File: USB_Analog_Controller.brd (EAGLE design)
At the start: 50 x 36 mm, 20 parts, among them J1 POWER, Q1 AO3400, Q2 AO3400, U1 PICO-MINI-02, U2 AP2112K, X1 PROG, X2 LED1, X3 LED2, X5 BOOT, X6 RESET

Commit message: Revision 2023-07-17
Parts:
- added R5, R6: 10K, M2M-Passives:R0603
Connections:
- net EN: now also R6.1
- net IO0: now also R5.1
- net L1: now also U1.12; no longer U1.9
- net L2: now also U1.13; no longer U1.10
- net VCC: now also R5.2, R6.2
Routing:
- net VCC: track 22.5 -> 33.6 mm
- net L1: track 10.8 -> 15.8 mm
- net EN: track 25.2 -> 26.8 mm
- net IO0: track 30.8 -> 32.2 mm
- net L2: track 13.6 -> 14.2 mm
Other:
- board text added: "2023-07-17"
- board text removed: "2023-06-03"
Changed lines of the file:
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@@
 <wire x1="23.5" y1="36" x2="2" y2="36" width="0" layer="20"/>
 <wire x1="2" y1="36" x2="0" y2="34" width="0" layer="20" curve="90"/>
-<text x="48.5" y="7" size="1.27" layer="21" rot="R90">USB Analog Controller</text>
-<text x="15.5" y="33.5" size="1.27" layer="21">2023-06-03</text>
+<text x="48.5" y="6" size="1.27" layer="21" rot="R90">USB Analog
+Controller</text>
+<text x="48.5" y="20" size="1.016" layer="21" rot="R90">2023-07-17</text>
 </plain>
 <attributes>
@@
 <attribute name="NAME" x="29.9275" y="2.23" size="1.016" layer="26" rot="R90"/>
 <attribute name="NAME" x="38.5" y="4.135" size="1.27" layer="51" rot="R180" align="bottom-center"/>
-<attribute name="VALUE" x="30.73" y="0.975" size="1.016" layer="27"/>
+<attribute name="VALUE" x="30.73" y="0.975" size="1.016" layer="21"/>
 </element>
 <element name="X2" library="M2M-Connectors" package="USB-A-SS-52100-001" value="LED1" x="10" y="27" smashed="yes" rot="R90">
@@
 </element>
 <element name="X5" library="M2M-Connectors" package="1X02-2.54" value="BOOT" x="25.5" y="3.5" smashed="yes">
-<attribute name="NAME" x="24.611" y="2.865" size="1.27" layer="48"/>
 <attribute name="NAME" x="24.865" y="2.865" size="0.8128" layer="51"/>
 <attribute name="NAME" x="24.23" y="5.0875" size="1.016" layer="25"/>
-<attribute name="VALUE" x="24.23" y="0.96" size="1.016" layer="27"/>
+<attribute name="NAME" x="24.611" y="2.865" size="1.27" layer="48"/>
+<attribute name="VALUE" x="24.23" y="0.96" size="1.016" layer="21"/>
 </element>
 <element name="X6" library="M2M-Connectors" package="1X02-2.54" value="RESET" x="19" y="3.5" smashed="yes">
-<attribute name="NAME" x="18.111" y="2.865" size="1.27" layer="48"/>
 <attribute name="NAME" x="18.865" y="2.365" size="0.8128" layer="51"/>
 <attribute name="NAME" x="17.73" y="5.0875" size="1.016" layer="25"/>
-<attribute name="VALUE" x="17.73" y="0.96" size="1.016" layer="27"/>
+<attribute name="NAME" x="18.111" y="2.865" size="1.27" layer="48"/>
+<attribute name="VALUE" x="17.73" y="0.96" size="1.016" layer="21"/>
 </element>
 <element name="J1" library="M2M-Connectors" package="TERMINAL-5.08-2P" value="POWER" x="36" y="11.5" smashed="yes"/>
@@
 <element name="U$1" library="M2M-Frames" package="BERGDAHL-20MM-BPLACE" value="" x="21" y="25.5" smashed="yes" rot="R270"/>
 <element name="U$2" library="M2M-Frames" package="OSHW-8MM-BPLACE" value="" x="35.5" y="17.5" smashed="yes" rot="R270"/>
+<element name="R5" library="M2M-Passives" package="R0603" value="10K" x="28.5" y="6.5" smashed="yes" rot="R180">
+<attribute name="NAME" x="28.5" y="5.5475" size="1.016" layer="25" rot="R180" align="bottom-center"/>
+<attribute name="NAME" x="28.5" y="6.5" size="0.6096" layer="51" rot="R180" align="center"/>
+<attribute name="VALUE" x="28.5" y="8.405" size="1.016" layer="27" rot="R180" align="bottom-center"/>
+</element>
+<element name="R6" library="M2M-Passives" package="R0603" value="10K" x="25.5" y="6.5" smashed="yes">
+<attribute name="NAME" x="25.5" y="7.4525" size="1.016" layer="25" align="bottom-center"/>
+<attribute name="NAME" x="25.5" y="6.5" size="0.6096" layer="51" align="center"/>
+<attribute name="VALUE" x="25.5" y="4.595" size="1.016" layer="27" align="bottom-center"/>
+</element>
 </elements>
 <signals>
@@
 <wire x1="29" y1="22.5" x2="24" y2="27.5" width="0.4064" layer="16"/>
 <wire x1="24" y1="27.5" x2="23.5" y2="27.5" width="0.4064" layer="16"/>
+<contactref element="R5" pad="2"/>
+<contactref element="R6" pad="2"/>
+<wire x1="26.35" y1="6.5" x2="26.5" y2="6.5" width="0.254" layer="1"/>
+<wire x1="26.5" y1="6.5" x2="27.65" y2="6.5" width="0.254" layer="1"/>
+<wire x1="26.55" y1="14.2" x2="24" y2="11.65" width="0.254" layer="1"/>
+<wire x1="24" y1="9" x2="26.5" y2="6.5" width="0.254" layer="1"/>
+<wire x1="24" y1="11.65" x2="24" y2="9" width="0.254" layer="1"/>
 </signal>
 <signal name="GND">
@@
 <via x="40" y="18.5" extent="1-16" drill="0.35"/>
 <via x="31" y="18.5" extent="1-16" drill="0.35"/>
-<via x="27" y="18.5" extent="1-16" drill="0.35"/>
+<via x="27.119" y="19.643" extent="1-16" drill="0.35"/>
 <via x="47.5" y="2.5" extent="1-16" drill="0.35"/>
 <via x="43.5" y="10.5" extent="1-16" drill="0.35"/>
@@
 <via x="9.5" y="8" extent="1-16" drill="0.35"/>
 <via x="29.5" y="16" extent="1-16" drill="0.35"/>
-<via x="29.5" y="7.5" extent="1-16" drill="0.35"/>
+<via x="31" y="8.5" extent="1-16" drill="0.35"/>
 <via x="25" y="10" extent="1-16" drill="0.35"/>
 <via x="21.5" y="8.5" extent="1-16" drill="0.35"/>
@@
 <wire x1="41" y1="7" x2="41" y2="16" width="0.254" layer="1"/>
 <wire x1="41" y1="16" x2="38" y2="19" width="0.254" layer="1"/>
-<wire x1="27.5" y1="5.5" x2="39.5" y2="5.5" width="0.254" layer="1"/>
+<wire x1="27.5" y1="5.5" x2="30.35" y2="5.5" width="0.254" layer="1"/>
+<contactref element="R5" pad="1"/>
+<wire x1="30.5" y1="5.5" x2="39.5" y2="5.5" width="0.254" layer="1"/>
+<wire x1="29.35" y1="6.5" x2="30.35" y2="5.5" width="0.254" layer="1"/>
+<wire x1="30.35" y1="5.5" x2="30.5" y2="5.5" width="0.254" layer="1"/>
 </signal>
 <signal name="EN">
 <contactref element="U1" pad="8"/>
 <contactref element="X6" pad="1"/>
-<wire x1="28.1" y1="22.9" x2="27.1" y2="22.9" width="0.254" layer="1"/>
-<wire x1="27.1" y1="22.9" x2="26.5" y2="23.5" width="0.254" layer="1"/>
-<via x="26.5" y="23.5" extent="1-16" drill="0.35"/>
-<wire x1="26.5" y1="23.5" x2="26.5" y2="20.5" width="0.254" layer="16"/>
-<via x="26.5" y="20.5" extent="1-16" drill="0.35"/>
+<wire x1="28.1" y1="22.9" x2="27.4" y2="22.9" width="0.254" layer="1"/>
+<wire x1="27.4" y1="22.9" x2="26.5" y2="22" width="0.254" layer="1"/>
+<via x="26.5" y="22" extent="1-16" drill="0.35"/>
+<wire x1="26.5" y1="22" x2="26.5" y2="17.5" width="0.254" layer="16"/>
+<via x="26.5" y="17.5" extent="1-16" drill="0.35"/>
 <wire x1="23" y1="7.5" x2="19" y2="3.5" width="0.254" layer="1"/>
-<wire x1="26.5" y1="20.5" x2="26" y2="20.5" width="0.254" layer="1"/>
-<wire x1="26" y1="20.5" x2="23" y2="17.5" width="0.254" layer="1"/>
-<wire x1="23" y1="17.5" x2="23" y2="7.5" width="0.254" layer="1"/>
+<wire x1="26.5" y1="17.5" x2="24.5" y2="17.5" width="0.254" layer="1"/>
+<wire x1="24.5" y1="17.5" x2="23" y2="16" width="0.254" layer="1"/>
+<wire x1="23" y1="16" x2="23" y2="7.5" width="0.254" layer="1"/>
+<contactref element="R6" pad="1"/>
+<wire x1="24.65" y1="6.5" x2="24" y2="6.5" width="0.254" layer="1"/>
+<wire x1="24" y1="6.5" x2="23" y2="7.5" width="0.254" layer="1"/>
 </signal>
 <signal name="TXD0">
@@
 </signal>
 <signal name="L1">
-<contactref element="U1" pad="9"/>
 <contactref element="R1" pad="1"/>
-<wire x1="26.9" y1="22.1" x2="28.1" y2="22.1" width="0.254" layer="1"/>
-<wire x1="19.35" y1="27" x2="22" y2="27" width="0.254" layer="1"/>
-<wire x1="22" y1="27" x2="26.9" y2="22.1" width="0.254" layer="1"/>
+<wire x1="21.5" y1="27" x2="19.35" y2="27" width="0.254" layer="1"/>
+<contactref element="U1" pad="12"/>
+<wire x1="29.2" y1="19.6" x2="29.2" y2="19.2132" width="0.254" layer="1"/>
+<wire x1="29.2" y1="19.2132" x2="28.5" y2="18.5132" width="0.254" layer="1"/>
+<wire x1="28.5" y1="18.5132" x2="26.9868" y2="18.5132" width="0.254" layer="1"/>
+<wire x1="26.9868" y1="18.5132" x2="25" y2="20.5" width="0.254" layer="1"/>
+<wire x1="25" y1="20.5" x2="25" y2="23.5" width="0.254" layer="1"/>
+<wire x1="25" y1="23.5" x2="21.5" y2="27" width="0.254" layer="1"/>
 </signal>
 <signal name="L2">
-<contactref element="U1" pad="10"/>
 <contactref element="R2" pad="1"/>
-<wire x1="28.1" y1="21.3" x2="25.3" y2="21.3" width="0.254" layer="1"/>
-<wire x1="19.35" y1="15.35" x2="19.35" y2="13" width="0.254" layer="1"/>
-<wire x1="25.3" y1="21.3" x2="19.35" y2="15.35" width="0.254" layer="1"/>
+<wire x1="19.35" y1="13" x2="19.35" y2="13.85" width="0.254" layer="1"/>
+<contactref element="U1" pad="13"/>
+<wire x1="30" y1="19" x2="30" y2="19.6" width="0.254" layer="1"/>
+<wire x1="19.35" y1="13.85" x2="23.6068" y2="18.1068" width="0.254" layer="1"/>
+<wire x1="23.6068" y1="18.1068" x2="29.1068" y2="18.1068" width="0.254" layer="1"/>
+<wire x1="29.1068" y1="18.1068" x2="30" y2="19" width="0.254" layer="1"/>
 </signal>
 <signal name="NC">

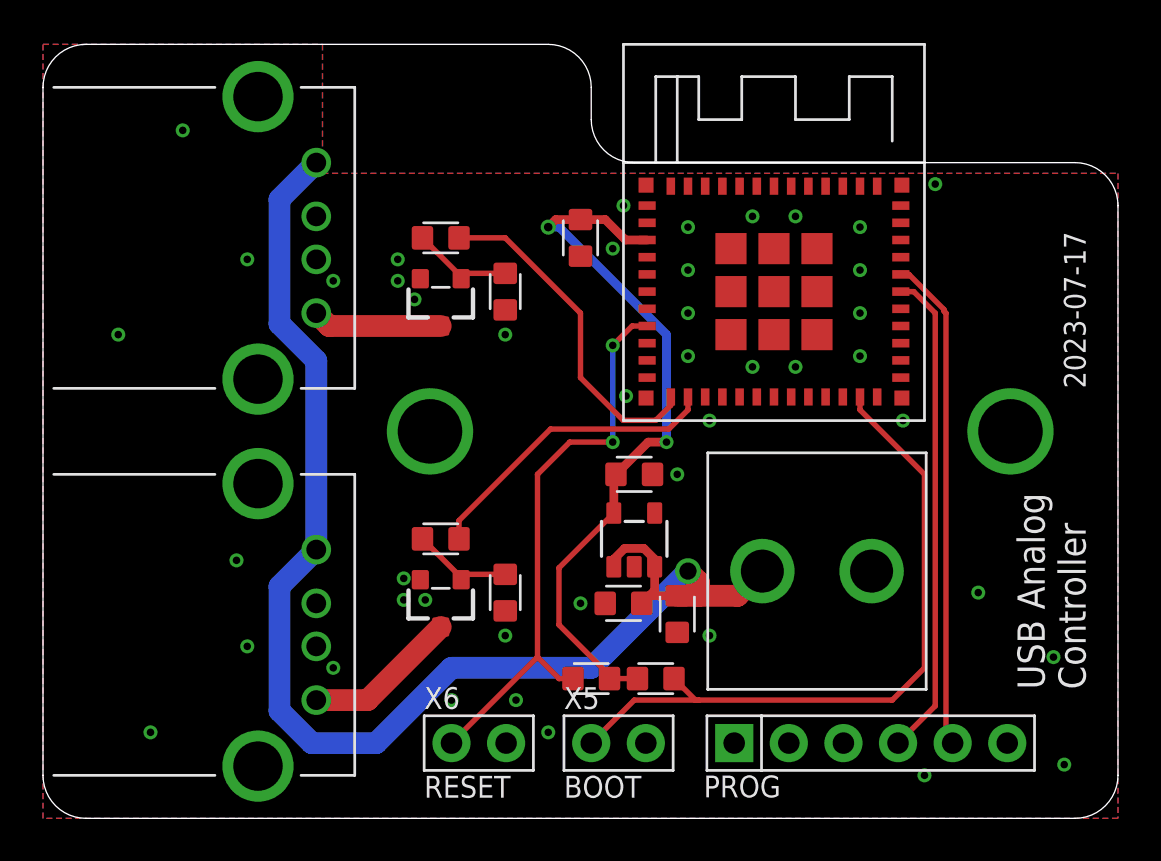
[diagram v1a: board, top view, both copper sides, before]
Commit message: Added PTC fuse
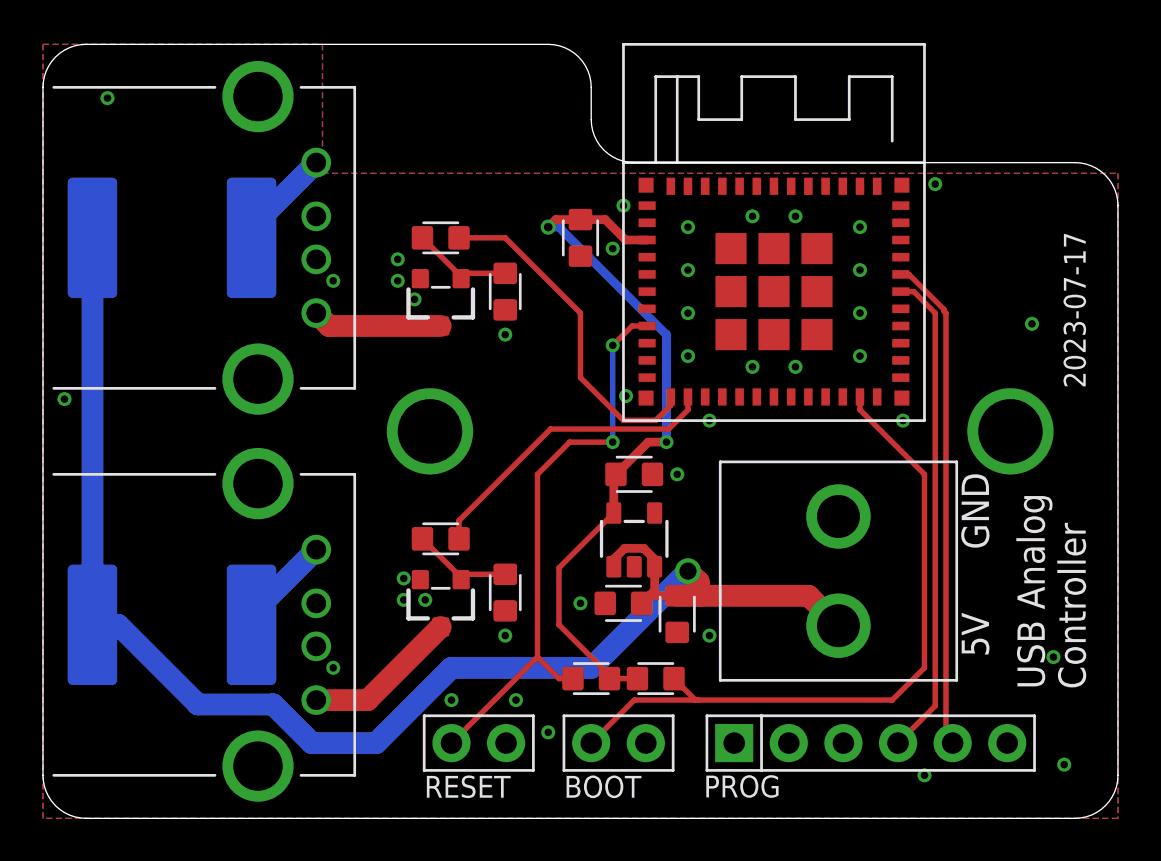
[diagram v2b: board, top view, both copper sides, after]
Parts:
- added F1, F2: 3A, M2M-Fuse:JK-SMD300
- moved J1 1.00 mm to (37.0, 11.5), turned to 90 degrees
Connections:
- new net N$5: F1.B, X2.1
- new net N$6: F2.B, X3.1
- net VIN: now also F1.A, F2.A; no longer X2.1, X3.1
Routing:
- net N$6: track 0.00 -> 4.75 mm
- net N$5: track 0.00 -> 4.75 mm
- net VIN: track 63.1 -> 67.5 mm
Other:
- board text added: "5V"
- board text added: "GND"
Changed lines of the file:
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@@
 Controller</text>
 <text x="48.5" y="20" size="1.016" layer="21" rot="R90">2023-07-17</text>
+<text x="44" y="12.5" size="1.27" layer="21" rot="R90">GND</text>
+<text x="44" y="7.5" size="1.27" layer="21" rot="R90">5V</text>
 </plain>
 <attributes>
@@
 </element>
 <element name="X5" library="M2M-Connectors" package="1X02-2.54" value="BOOT" x="25.5" y="3.5" smashed="yes">
-<attribute name="NAME" x="24.865" y="2.865" size="0.8128" layer="51"/>
 <attribute name="NAME" x="24.23" y="5.0875" size="1.016" layer="25"/>
 <attribute name="NAME" x="24.611" y="2.865" size="1.27" layer="48"/>
+<attribute name="NAME" x="24.865" y="2.865" size="0.8128" layer="51"/>
 <attribute name="VALUE" x="24.23" y="0.96" size="1.016" layer="21"/>
 </element>
 <element name="X6" library="M2M-Connectors" package="1X02-2.54" value="RESET" x="19" y="3.5" smashed="yes">
-<attribute name="NAME" x="18.865" y="2.365" size="0.8128" layer="51"/>
 <attribute name="NAME" x="17.73" y="5.0875" size="1.016" layer="25"/>
 <attribute name="NAME" x="18.111" y="2.865" size="1.27" layer="48"/>
+<attribute name="NAME" x="18.865" y="2.365" size="0.8128" layer="51"/>
 <attribute name="VALUE" x="17.73" y="0.96" size="1.016" layer="21"/>
 </element>
-<element name="J1" library="M2M-Connectors" package="TERMINAL-5.08-2P" value="POWER" x="36" y="11.5" smashed="yes"/>
+<element name="J1" library="M2M-Connectors" package="TERMINAL-5.08-2P" value="POWER" x="37" y="11.5" smashed="yes" rot="R90"/>
 <element name="U2" library="M2M-IC" package="SOT23-5" value="AP2112K" x="27.5" y="13" smashed="yes">
 <attribute name="NAME" x="27.495" y="14.805" size="1.016" layer="25" align="bottom-center"/>
@@
 <attribute name="NAME" x="25.5" y="6.5" size="0.6096" layer="51" align="center"/>
 <attribute name="VALUE" x="25.5" y="4.595" size="1.016" layer="27" align="bottom-center"/>
+</element>
+<element name="F1" library="M2M-Fuse" package="JK-SMD300" value="3A" x="6" y="27" smashed="yes" rot="MR180">
+<attribute name="NAME" x="1" y="23.5" size="1.016" layer="26" rot="MR180"/>
+<attribute name="NAME" x="6" y="27" size="1.016" layer="48" rot="MR180" align="center"/>
+<attribute name="VALUE" x="1" y="31.5" size="1.016" layer="28" rot="MR180"/>
+</element>
+<element name="F2" library="M2M-Fuse" package="JK-SMD300" value="3A" x="6" y="9" smashed="yes" rot="MR180">
+<attribute name="NAME" x="1" y="5.5" size="1.016" layer="26" rot="MR180"/>
+<attribute name="NAME" x="6" y="9" size="1.016" layer="48" rot="MR180" align="center"/>
+<attribute name="VALUE" x="1" y="13.5" size="1.016" layer="28" rot="MR180"/>
 </element>
 </elements>
@@
 <via x="27.119" y="19.643" extent="1-16" drill="0.35"/>
 <via x="47.5" y="2.5" extent="1-16" drill="0.35"/>
-<via x="43.5" y="10.5" extent="1-16" drill="0.35"/>
+<via x="46" y="23" extent="1-16" drill="0.35"/>
 <via x="47" y="7.5" extent="1-16" drill="0.35"/>
 <via x="41" y="2" extent="1-16" drill="0.35"/>
@@
 <via x="22" y="5.5" extent="1-16" drill="0.35"/>
 <via x="19" y="5.5" extent="1-16" drill="0.35"/>
-<via x="5" y="4" extent="1-16" drill="0.35"/>
-<via x="9" y="12" extent="1-16" drill="0.35"/>
-<via x="3.5" y="22.5" extent="1-16" drill="0.35"/>
-<via x="6.5" y="32" extent="1-16" drill="0.35"/>
+<via x="1" y="19.5" extent="1-16" drill="0.35"/>
+<via x="3" y="33.5" extent="1-16" drill="0.35"/>
 <via x="16.5" y="25" extent="1-16" drill="0.35"/>
 <via x="16.5" y="26" extent="1-16" drill="0.35"/>
@@
 <via x="13.5" y="7" extent="1-16" drill="0.35"/>
 <via x="13.5" y="25" extent="1-16" drill="0.35"/>
-<via x="9.5" y="26" extent="1-16" drill="0.35"/>
-<via x="9.5" y="8" extent="1-16" drill="0.35"/>
 <via x="29.5" y="16" extent="1-16" drill="0.35"/>
 <via x="31" y="8.5" extent="1-16" drill="0.35"/>
@@
 <contactref element="C3" pad="1"/>
 <contactref element="U2" pad="3"/>
-<contactref element="X2" pad="1"/>
-<contactref element="X3" pad="1"/>
 <contactref element="C2" pad="1"/>
-<wire x1="33.46" y1="11.5" x2="32.31" y2="10.35" width="1.016" layer="1"/>
-<wire x1="32.31" y1="10.35" x2="30.5" y2="10.35" width="1.016" layer="1"/>
 <wire x1="30.5" y1="10.35" x2="29.5" y2="10.35" width="1.016" layer="1"/>
 <via x="30" y="11.5" extent="1-16" drill="0.8"/>
@@
 <wire x1="27.85" y1="10" x2="28.2" y2="10.35" width="0.4064" layer="1"/>
 <wire x1="28.2" y1="10.35" x2="29.5" y2="10.35" width="0.4064" layer="1"/>
-<wire x1="12.71" y1="12.5" x2="12.71" y2="21.29" width="1.016" layer="16"/>
-<wire x1="11" y1="23" x2="11" y2="28.79" width="1.016" layer="16"/>
-<wire x1="11" y1="28.79" x2="12.71" y2="30.5" width="1.016" layer="16"/>
-<wire x1="12.71" y1="21.29" x2="11" y2="23" width="1.016" layer="16"/>
-<wire x1="12.71" y1="12.5" x2="11" y2="10.79" width="1.016" layer="16"/>
-<wire x1="11" y1="10.79" x2="11" y2="5" width="1.016" layer="16"/>
-<wire x1="11" y1="5" x2="12.5" y2="3.5" width="1.016" layer="16"/>
 <wire x1="12.5" y1="3.5" x2="15.5" y2="3.5" width="1.016" layer="16"/>
 <wire x1="25.5" y1="7" x2="30" y2="11.5" width="1.016" layer="16"/>
@@
 <wire x1="28.45" y1="12.0516375" x2="27.9460375" y2="12.5556" width="0.4064" layer="1"/>
 <wire x1="27.9460375" y1="12.5556" x2="27.0539625" y2="12.5556" width="0.4064" layer="1"/>
+<contactref element="F1" pad="A"/>
+<contactref element="F2" pad="A"/>
+<wire x1="10.7" y1="5.3" x2="12.5" y2="3.5" width="1.016" layer="16"/>
+<wire x1="2.3" y1="27" x2="2.3" y2="9" width="1.016" layer="16"/>
+<wire x1="2.3" y1="9" x2="3.5" y2="9" width="1.016" layer="16"/>
+<wire x1="7.2" y1="5.3" x2="10.7" y2="5.3" width="1.016" layer="16"/>
+<wire x1="3.5" y1="9" x2="7.2" y2="5.3" width="1.016" layer="16"/>
+<wire x1="35.61" y1="10.35" x2="37" y2="8.96" width="1.016" layer="1"/>
+<wire x1="30.5" y1="10.35" x2="35.61" y2="10.35" width="1.016" layer="1"/>
+</signal>
+<signal name="N$5">
+<contactref element="X2" pad="1"/>
+<contactref element="F1" pad="B"/>
+<wire x1="12.71" y1="30.5" x2="9.7" y2="27.49" width="1.016" layer="16"/>
+<wire x1="9.7" y1="27.49" x2="9.7" y2="27" width="1.016" layer="16"/>
+</signal>
+<signal name="N$6">
+<contactref element="X3" pad="1"/>
+<contactref element="F2" pad="B"/>
+<wire x1="12.71" y1="12.5" x2="9.7" y2="9.49" width="1.016" layer="16"/>
+<wire x1="9.7" y1="9.49" x2="9.7" y2="9" width="1.016" layer="16"/>
 </signal>
 </signals>
